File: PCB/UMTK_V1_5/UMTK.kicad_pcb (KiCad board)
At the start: 2 copper layers, 88 parts, among them J1 Motor Out, J2 Motor Shunt, J3 JST 4pin, J4 Power IN, J5 PJ-102BH, J6 JST 4pin, J7 47589-0001, J8 10033526-N3212LF, Q1 Q_PNP_BEC, U1 DRV8873SPWPRQ1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

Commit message: Updated DRC and pcb
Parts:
- moved U6 4.66 mm to (106.0, 47.6)
- moved U2 2.70 mm to (134.6, 137.8)
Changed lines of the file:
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@@
 	(footprint "Package_SO:SOIC-24W_7.5x15.4mm_P1.27mm"
 		(layer "F.Cu")
-		(at 106.02 52.28)
+		(at 106.02 47.625)
 		(descr "SOIC, 24 Pin (JEDEC MS-013AD, https://www.analog.com/media/en/package-pcb-resources/package/pkg_pdf/soic_wide-rw/RW_24.pdf), generated with kicad-footprint-generator ipc_gullwing_generator.py")
 		(tags "SOIC SO")
@@
 	(footprint "Package_SO:SOP-16_3.9x9.9mm_P1.27mm"
 		(layer "F.Cu")
-		(at 135.89 135.43)
+		(at 134.58 137.795)
 		(descr "SOP, 16 Pin (https://www.diodes.com/assets/Datasheets/PAM8403.pdf), generated with kicad-footprint-generator ipc_gullwing_generator.py")
 		(tags "SOP SO")

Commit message: Initial Place, Board Stack
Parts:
- removed A1: Arduino_Mega2560_R3_Shield, arduino-library:Arduino_Mega2560_R3_Shield
- removed J6: JST 4pin, Connector_JST:JST_XH_B4B-XH-A_1x04_P2.50mm_Vertical
- removed J7: 47589-0001, digikey-footprints:USB_Micro_AB_Female_0475890001
- added A2: Clone_Mega2560_Pro_Socket, arduino-library:Clone_Mega2560_Pro_Socket, F.Cu at (52.1, 41.3)
- added JP3: Slide Logic LVL, Jumper:SolderJumper-3_P1.3mm_Bridged12_Pad1.0x1.5mm, F.Cu at (147.6, 66.0)
- C10, C12, C8, C9: footprint Diode_SMD:D_1206_3216Metric -> Capacitor_SMD:C_0603_1608Metric
- C13, C16: footprint Diode_SMD:D_1206_3216Metric -> Capacitor_SMD:C_0805_2012Metric
- J2: value Motor Shunt -> ESTOP
- J8: footprint digikey-footprints:USB_Mini_B_Female_548190519 -> Connector_USB:USB_Mini-B_Wuerth_65100516121_Horizontal
- moved U10 124.1 mm to (206.3, 108.0)
- moved C12 108.5 mm to (214.6, 72.4)
- moved R4 100.0 mm to (30.0, 78.7)
- moved R3 100.0 mm to (30.0, 76.2)
- moved R1 100.0 mm to (30.0, 72.2)
- moved R2 100.0 mm to (30.0, 74.2)
- moved C10 92.8 mm to (192.0, 62.2), turned to 90 degrees
- moved JP1 92.6 mm to (37.5, 64.8)
- moved R8 91.8 mm to (41.4, 77.5)
- moved R7 91.7 mm to (41.4, 74.9)
- moved R6 91.7 mm to (41.4, 72.9)
- moved J1 90.2 mm to (179.4, 50.1)
- moved C18 87.9 mm to (179.8, 121.9)
- moved C19 87.9 mm to (181.0, 127.8)
- moved C7 87.9 mm to (210.8, 135.1)
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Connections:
- J1 pad 1: /MotorDriver/VM- -> /MotorDriver/VM+
- J1 pad 2: /MotorDriver/VM+ -> /MotorDriver/VM-
- J4 pad 1: +12V -> GND
- J4 pad 2: GND -> +12V
- J5 pad 2: unconnected-(J5-Pad2) -> GND
- J8 pad 3: /Linear Slide/_SLIDE_CLK -> /Linear Slide/_SLIDE_CLK_
- U1 pad 25: unconnected-(U1-EP-Pad25)_16 -> GND
- U11 pad 4: /Linear Slide/_SLIDE_CLK -> /Linear Slide/_SLIDE_CLK_
- U11 pad 6: +5V -> /Linear Slide/_SLIDE_DATA_LVL_
- U12 pad 4: /Linear Slide/_SLIDE_CLK -> /Linear Slide/_SLIDE_DAT_
- U12 pad 6: +5V -> /Linear Slide/_SLIDE_DATA_LVL_
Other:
- copper layers 2 -> 4
- board text added: "DISPLACMENT (MM)"
- board text added: "ESTOP"
- board text added: "FORCE (NEWTONS)"
- board text added: "LOADCELL"
- board text added: "MOTOR"
- board text added: "POWER"
- board text added: "SLIDE"

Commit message: Layout Started
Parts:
- moved R29 107.0 mm to (65.9, 31.6)
- moved R31 107.0 mm to (65.9, 35.5)
- moved C13 107.0 mm to (70.2, 30.3)
- moved C14 107.0 mm to (71.7, 21.8)
- moved R28 107.0 mm to (65.9, 29.6)
- moved R30 107.0 mm to (65.9, 33.5)
- moved C15 107.0 mm to (71.7, 23.7)
- moved C16 107.0 mm to (70.2, 33.7)
- moved R32 107.0 mm to (65.9, 37.5)
- moved C7 106.3 mm to (141.9, 54.0), turned to 180 degrees
- moved U3 102.2 mm to (22.9, 101.4), turned to -90 degrees
- moved U5 99.1 mm to (22.9, 105.8), turned to -90 degrees
- moved U12 97.1 mm to (24.1, 57.1), turned to -90 degrees
- moved U4 96.4 mm to (22.9, 110.3), turned to -90 degrees
- moved Q1 92.6 mm to (74.0, 51.8)
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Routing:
- net GND: track 0.00 -> 1.44 mm
- net (no net): vias 0 -> 6
- added copper zone on F.Cu, net /MotorDriver/VM-
- added copper zone on In1.Cu, net /MotorDriver/VM-
- added copper zone on F.Cu, net GND
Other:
- rule pad_to_mask_clearance: 0 -> 0.05

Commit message: Layout Continue
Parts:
- removed C20: 220u, Capacitor_SMD:CP_Elec_10x10
- removed C22: 1000u, Capacitor_SMD:CP_Elec_10x10
- removed J4: Power IN, TerminalBlock_Altech:Altech_AK100_1x02_P5.00mm
- removed U9: LD1117AS33TR, Package_TO_SOT_SMD:SOT-223
- added U13: TLV76133DCY, Package_TO_SOT_SMD:SOT-223-3_TabPin2, F.Cu at (128.7, 88.4)
- C18: value 220u -> 10u; footprint Capacitor_SMD:CP_Elec_8x6.5 -> Capacitor_SMD:C_0805_2012Metric
- C19: value 0.1u -> 10u; footprint Capacitor_SMD:C_0402_1005Metric -> Capacitor_SMD:C_0805_2012Metric
- C21: footprint Capacitor_SMD:CP_Elec_10x10 -> Capacitor_SMD:CP_Elec_8x10.5
- moved J5 109.4 mm to (137.4, 49.0)
- moved C17 90.0 mm to (130.3, 72.6), turned to -90 degrees
- moved C19 72.7 mm to (121.7, 85.9), turned to -90 degrees
- moved C18 66.1 mm to (121.7, 90.4), turned to -90 degrees
- moved D1 62.8 mm to (135.6, 81.0), turned to 180 degrees
- moved R23 58.9 mm to (171.5, 87.7)
- moved R26 58.9 mm to (175.0, 84.0)
- moved RDNP1 58.9 mm to (171.5, 93.7)
- moved R22 58.9 mm to (171.5, 85.7)
- moved R25 58.9 mm to (171.5, 91.7)
- moved R27 58.9 mm to (175.0, 86.5)
- moved R21 58.9 mm to (171.5, 83.7)
- moved R24 58.9 mm to (171.5, 89.7)
- moved C21 56.2 mm to (159.8, 79.2), turned to 90 degrees
- moved C12 33.9 mm to (186.8, 91.7)
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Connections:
- C18 pad 1: +5V -> GND
- C18 pad 2: GND -> +5V
- C19 pad 1: +3V3 -> GND
- C19 pad 2: GND -> +3V3
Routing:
- net +5V: track 0.00 -> 50.9 mm
- net Net-(D1-K): track 0.00 -> 22.1 mm
- net GND: track 1.44 -> 17.6 mm, vias 0 -> 50
- net Net-(U1-VCP): track 0.00 -> 6.62 mm
- net +3V3: track 0.00 -> 6.30 mm
- net Net-(U1-CPL): track 0.00 -> 3.13 mm
- net Net-(U1-CPH): track 0.00 -> 2.64 mm
- net VMOTOR: vias 0 -> 29
- net /MotorDriver/VM-: vias 0 -> 9
- net /MotorDriver/VM+: vias 0 -> 9
- net (no net): vias 6 -> 43
- added copper zone on F.Cu, net +5V
- added copper zone on F.Cu, net /MotorDriver/VM+
- added copper zone on In1.Cu, net /MotorDriver/VM+
- added copper zone on B.Cu, net GND
- added copper zone on In1.Cu, net GND
- added copper zone on In2.Cu, net GND
- added copper zone on B.Cu, net VMOTOR
- added copper zone on F.Cu, net VMOTOR
- added copper zone on In1.Cu, net VMOTOR
- added copper zone on In2.Cu, net VMOTOR

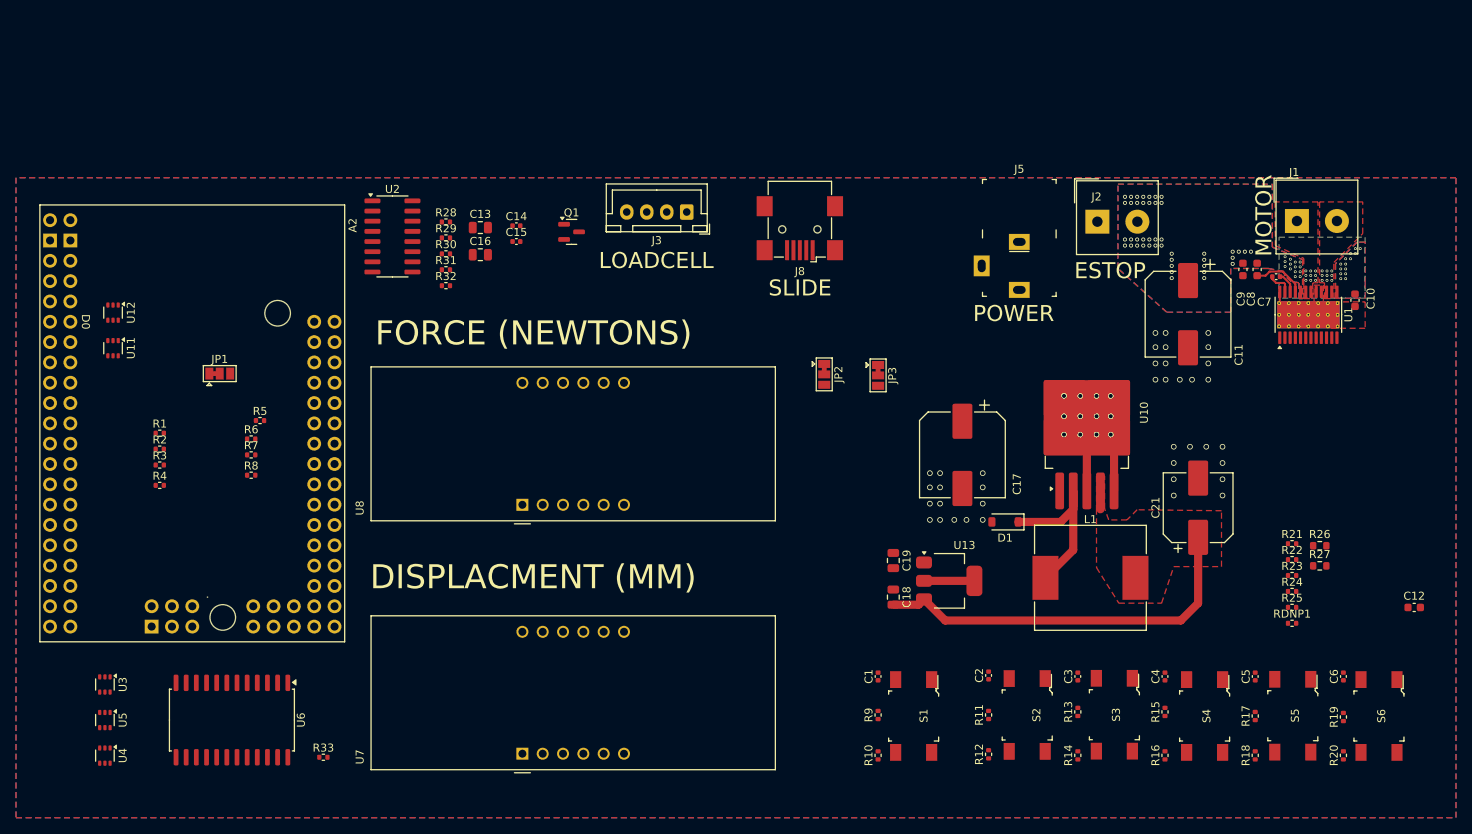
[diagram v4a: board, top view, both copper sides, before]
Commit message: Placement Approved, Added holes
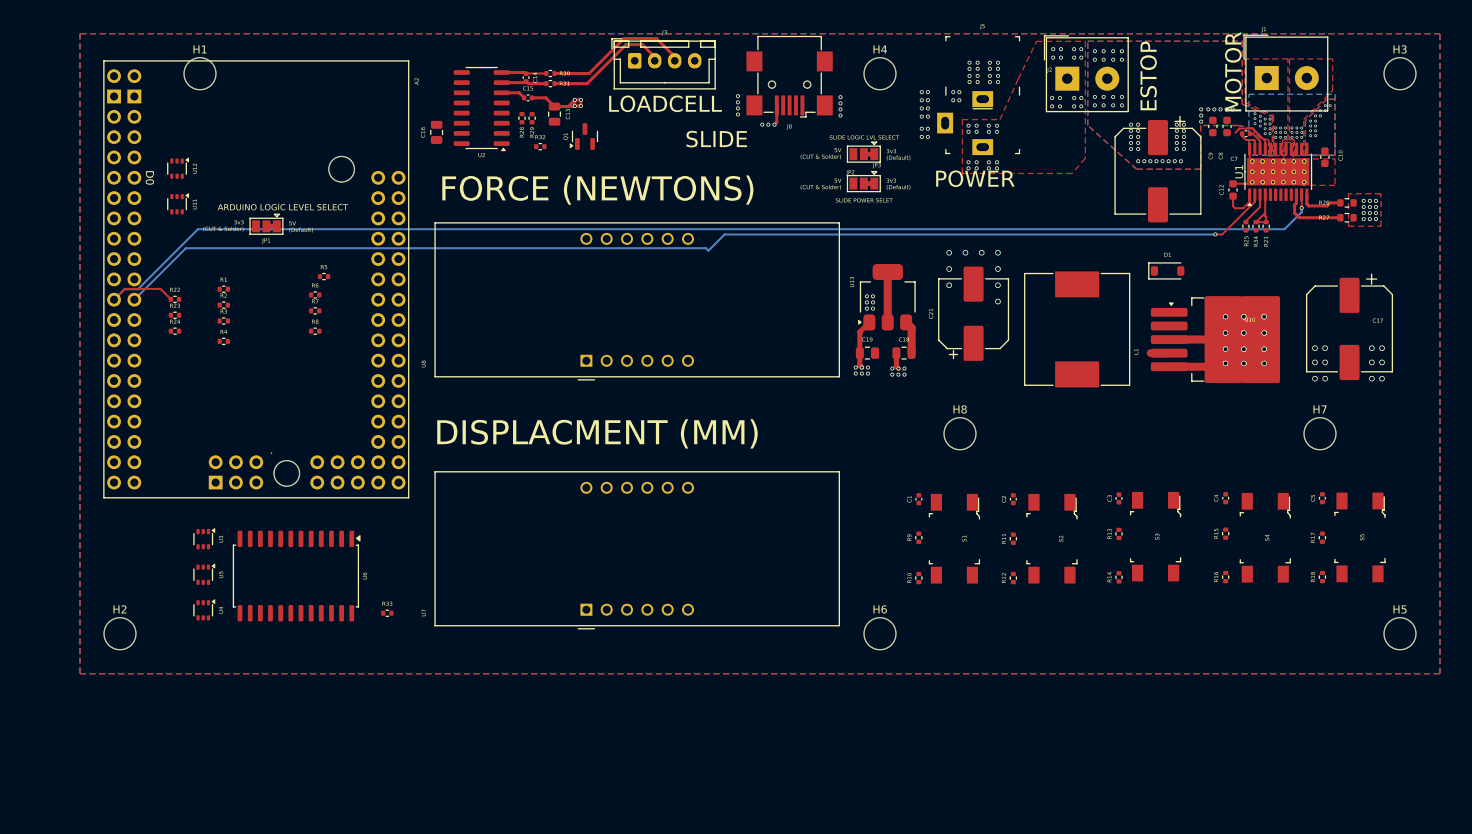
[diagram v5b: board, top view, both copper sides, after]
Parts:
- removed C6: 0.1u, Capacitor_SMD:C_0402_1005Metric
- removed R19: 10k, Resistor_SMD:R_0402_1005Metric
- removed R20: 100r, Resistor_SMD:R_0402_1005Metric
- removed S6: FSM4JSMATR, digikey-footprints:Switch_Tactile_SMD_6x6mm
- added H1: MountingHole, MountingHole:MountingHole_4mm, F.Cu at (35.0, 25.0)
- added H2: MountingHole, MountingHole:MountingHole_4mm, F.Cu at (25.0, 95.0)
- added H3: MountingHole, MountingHole:MountingHole_4mm, F.Cu at (185.0, 25.0)
- added H4: MountingHole, MountingHole:MountingHole_4mm, F.Cu at (120.0, 25.0)
- added H5: MountingHole, MountingHole:MountingHole_4mm, F.Cu at (185.0, 95.0)
- added H6: MountingHole, MountingHole:MountingHole_4mm, F.Cu at (120.0, 95.0)
- added H7: MountingHole, MountingHole:MountingHole_4mm, F.Cu at (175.0, 70.0)
- added H8: MountingHole, MountingHole:MountingHole_4mm, F.Cu at (130.0, 70.0)
- R34: renamed from RDNP1; value R_US -> DNP
- U1: footprint Package_SO:HTSSOP-24-1EP_4.4x7.8mm_P0.65mm_EP3.4x7.8mm_Mask2.4x2.98mm_ThermalVias -> Package_SO:HTSSOP-24-1EP_4.4x7.8mm_P0.65mm_EP3.4x7.8mm_Mask2.4x4.68mm_ThermalVias
- moved R22 143.4 mm to (31.9, 53.2)
- moved R23 143.4 mm to (31.9, 55.2)
- moved R24 143.4 mm to (31.9, 57.2)
- moved C12 56.9 mm to (164.1, 39.5), turned to 90 degrees
- moved C17 50.9 mm to (178.7, 56.9)
- moved R34 49.8 mm to (167.0, 44.1), turned to 90 degrees
- moved R25 48.0 mm to (165.7, 44.1), turned to 90 degrees
- moved R27 43.6 mm to (178.4, 43.0), turned to 180 degrees
- moved R26 43.0 mm to (178.4, 41.1), turned to 180 degrees
- moved R21 39.8 mm to (168.3, 44.1), turned to -90 degrees
- moved D1 37.4 mm to (156.0, 49.7), turned to 0 degrees
- moved C21 37.1 mm to (131.7, 55.0)
- moved U13 36.3 mm to (121.0, 52.9), turned to 90 degrees
- moved L1 31.1 mm to (144.6, 57.0), turned to -90 degrees
- moved C18 30.5 mm to (123.0, 59.9), turned to 0 degrees
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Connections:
- A2 pad A13: /Arduino/SW_6 -> unconnected-(A2-PadA13)
- JP1 pad 1: +3V3 -> +5V
- JP1 pad 3: +5V -> +3V3
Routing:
- net /Arduino/MOT_nSLEEP: track 0.00 -> 163.4 mm, vias 0 -> 1
- net /Arduino/MOT_nFAULT: track 0.00 -> 146.3 mm, vias 0 -> 1
- net +5V: track 50.9 -> 6.42 mm
- net GND: track 17.6 -> 42.2 mm, vias 50 -> 78
- net Net-(D1-K): track 22.1 -> 0.00 mm
- net /HX711/LCS+: track 0.00 -> 18.3 mm
- net /HX711/LCS-: track 0.00 -> 15.7 mm
- net /Arduino/MOT_SENSE1: track 0.00 -> 8.35 mm
- net /MotorDriver/SR - Slew Rate Adjust: track 0.00 -> 6.39 mm
- net Net-(U2-INA-): track 0.00 -> 5.77 mm
- net Net-(U2-INA+): track 0.00 -> 5.70 mm
- net /Arduino/MOT_SENSE2: track 0.00 -> 5.61 mm
- net Net-(U1-DVDD): track 0.00 -> 4.66 mm
- net /Arduino/MOT_MODE: track 0.00 -> 4.17 mm
- net Net-(U2-VBG): track 0.00 -> 3.09 mm
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- added copper zone on F.Cu, net +12V
- added copper zone on In1.Cu, net +12V
- removed copper zone on F.Cu, net +5V
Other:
- board text added: "3v3 (CUT & Solder)"
- board text added: "3v3 (Default)"
- board text added: "5V (CUT & Solder)"
- board text added: "5V (Default)"
- board text added: "ARDUINO LOGIC LEVEL SELECT"
- board text added: "SLIDE LOGIC LVL SELECT"
- board text added: "SLIDE POWER SELET"

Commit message: Routing
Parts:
- moved R33 25.2 mm to (33.5, 96.0), turned to 90 degrees
- moved U12 14.9 mm to (44.5, 28.5)
- moved U11 14.9 mm to (44.5, 33.0)
- moved R10 2.91 mm to (122.0, 87.5)
- moved C1 2.87 mm to (122.0, 78.5)
- moved R9 2.86 mm to (122.0, 83.0)
- moved R15 2.38 mm to (160.9, 83.0)
- moved C4 2.37 mm to (160.9, 78.5)
- moved R16 2.37 mm to (160.9, 87.5)
- moved S1 2.31 mm to (127.0, 83.0)
- moved S4 2.17 mm to (166.0, 83.1)
- moved R13 2.01 mm to (147.9, 83.0)
- moved R14 2.01 mm to (147.9, 87.5)
- moved C3 2.00 mm to (147.9, 78.5)
- moved R12 1.79 mm to (135.0, 87.5)
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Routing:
- net Net-(U6-SEG_A): track 0.00 -> 136.6 mm, vias 0 -> 3
- net Net-(U6-SEG_F): track 0.00 -> 132.5 mm, vias 0 -> 3
- net Net-(U6-SEG_B): track 0.00 -> 121.9 mm, vias 0 -> 2
- net /Arduino/SW_5: track 0.00 -> 98.8 mm, vias 0 -> 2
- net Net-(U6-SEG_G): track 0.00 -> 90.3 mm
- net /Arduino/SW_4: track 0.00 -> 88.5 mm, vias 0 -> 2
- net Net-(U6-DIG_1): track 0.00 -> 86.8 mm
- net Net-(U6-SEG_C): track 0.00 -> 84.7 mm
- net Net-(U6-SEG_DP): track 0.00 -> 81.4 mm
- net Net-(U6-SEG_D): track 0.00 -> 77.9 mm
- net /Arduino/SW_3: track 0.00 -> 73.3 mm, vias 0 -> 2
- net /Arduino/SW_2: track 0.00 -> 65.5 mm, vias 0 -> 2
- net Net-(U6-DIG_0): track 0.00 -> 62.2 mm, vias 0 -> 2
- net Net-(U6-DIG_5): track 0.00 -> 60.1 mm, vias 0 -> 2
- net Net-(U6-DIG_6): track 0.00 -> 54.7 mm
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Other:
- board text added: "DISPLACEMENT (MM)"
- board text removed: "DISPLACMENT (MM)"

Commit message: WIP laying board
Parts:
- moved JP1 104.8 mm to (145.0, 69.2)
- moved R1 104.0 mm to (141.1, 38.9), turned to 90 degrees
- moved R2 103.1 mm to (140.0, 38.9), turned to -90 degrees
- moved R3 102.3 mm to (138.8, 38.9), turned to 90 degrees
- moved R4 101.6 mm to (137.7, 38.9), turned to -90 degrees
- moved R6 97.4 mm to (145.8, 38.9), turned to -90 degrees
- moved R5 97.2 mm to (147.1, 38.9), turned to 90 degrees
- moved R7 96.4 mm to (144.5, 38.9), turned to 90 degrees
- moved R8 95.6 mm to (143.3, 38.9), turned to -90 degrees
- moved U12 21.1 mm to (46.1, 49.5), turned to 90 degrees
- moved U11 16.8 mm to (41.6, 49.5), turned to 90 degrees
- moved R33 5.31 mm to (37.5, 92.5)
- moved U4 2.41 mm to (33.0, 92.0)
- moved C16 0.60 mm to (64.0, 32.5)
- moved D1 0.18 mm to (156.1, 49.5)
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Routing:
- net /Arduino/Vin_Sense: track 0.00 -> 96.3 mm
- net /Arduino/VM_Sense: track 0.00 -> 94.2 mm
- net Net-(U6-DIG_2): track 0.00 -> 81.4 mm
- net Net-(U6-DIG_7): track 0.00 -> 57.2 mm
- net Net-(U6-SEG_E): track 35.7 -> 78.5 mm
- net /Arduino/SW_2: track 65.5 -> 23.3 mm, vias 2 -> 1
- net /Arduino/SW_1: track 52.3 -> 10.2 mm, vias 2 -> 1
- net /Arduino/SW_4: track 88.5 -> 50.0 mm, vias 2 -> 1
- net /Arduino/SW_3: track 73.3 -> 36.7 mm, vias 2 -> 1
- net +3V3: track 6.30 -> 40.8 mm
- net /Arduino/SW_5: track 98.8 -> 66.3 mm, vias 2 -> 1
- net /HX711/LCE+: track 0.00 -> 29.7 mm
- net Net-(U6-DIG_3): track 52.0 -> 74.6 mm
- net /Linear Slide/SLIDE_PWR: track 0.00 -> 22.4 mm
- net +5V: track 10.0 -> 32.1 mm, vias 3 -> 10
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- added copper zone on F.Cu, net +5V
- added copper zone on In1.Cu, net +5V
- added copper zone on F.Cu, net Net-(D1-K)
- added copper zone on In1.Cu, net VDD
- removed copper zone on In1.Cu, net GND

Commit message: Update UMTK.kicad_pcb
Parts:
- moved U11 67.4 mm to (108.2, 38.9)
- moved U12 67.4 mm to (112.7, 38.9)
- moved U13 14.0 mm to (119.8, 66.9), turned to -90 degrees
- moved JP3 11.3 mm to (121.6, 45.7)
- moved JP2 11.1 mm to (121.8, 49.1)
- moved C18 5.27 mm to (117.7, 59.9), turned to 180 degrees
- moved C19 3.87 mm to (122.3, 59.9), turned to 180 degrees
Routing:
- net /Linear Slide/SLIDE_PWR: track 22.4 -> 0.00 mm
- net +3V3: track 40.8 -> 55.2 mm
- net /Linear Slide/_SLIDE_DAT_: track 0.00 -> 10.6 mm
- net /Linear Slide/_SLIDE_CLK_: track 0.00 -> 9.08 mm
- net +5V: track 32.1 -> 25.6 mm, vias 10 -> 22
- net /Arduino/SLIDE_DAT_DIR: track 16.1 -> 10.1 mm
- net /Arduino/SLIDE_CLK_DIR: track 15.6 -> 12.3 mm
- net (no net): vias 12 -> 0
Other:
- board text added: "5V CUT & Solder"
- board text added: "SLIDE ONLY ! NOT USB !"
- board text removed: "5V (CUT & Solder)"
- board text removed: "SLIDE"
